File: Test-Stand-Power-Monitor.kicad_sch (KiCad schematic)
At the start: 19 parts, among them J1 560020-0330, J2 Conn_01x02_Pin, J3 1715721, J4 Conn_01x03_Pin, J5 BM03B-GHS-TBT, U1 TLV75533PDBV, U2 AP63205WU-7, U3 ESP32-DevKitC, U4 TLP241A(TP1,F

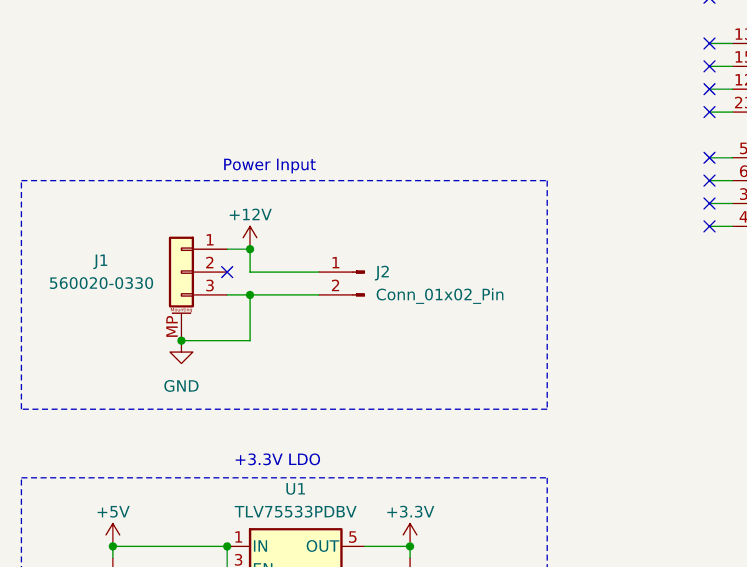
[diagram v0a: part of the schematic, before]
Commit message: Marked two-pin header as DNI to prevent short risk for +12V after testing.
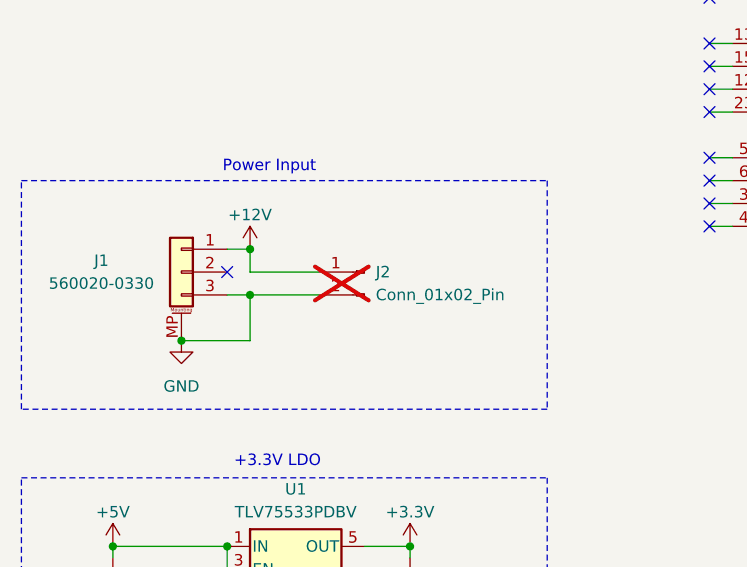
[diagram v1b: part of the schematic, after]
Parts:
- J2: now not fitted
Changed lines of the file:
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@@
   )
   (symbol (lib_id "Connector:Conn_01x02_Pin") (at 55.626 104.14 0) (mirror y) (unit 1)
-    (in_bom yes) (on_board yes) (dnp no)
+    (in_bom yes) (on_board yes) (dnp yes)
     (property "Reference" "J2" (at 56.896 104.14 0)
       (effects (font (size 1.27 1.27)) (justify right))

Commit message: Imported updated files from office verison of this project
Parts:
- J2: now fitted
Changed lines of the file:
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@@
   (title_block
     (title "Test Stand Power Monitor")
-    (date "2023-06-05")
+    (date "2023-08-08")
     (rev "1.0")
     (comment 1 "Ed Katynski")
@@
   )
   (symbol (lib_id "Connector:Conn_01x02_Pin") (at 55.626 104.14 0) (mirror y) (unit 1)
-    (in_bom yes) (on_board yes) (dnp yes)
+    (in_bom yes) (on_board yes) (dnp no)
     (property "Reference" "J2" (at 56.896 104.14 0)
       (effects (font (size 1.27 1.27)) (justify right))
